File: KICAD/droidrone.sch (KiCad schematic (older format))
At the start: 58 parts, among them IC1 ATMEGA328PB, P1 USB_A, U1 TA4805S, U4 LP2950L-3.3V, Y1 Crystal

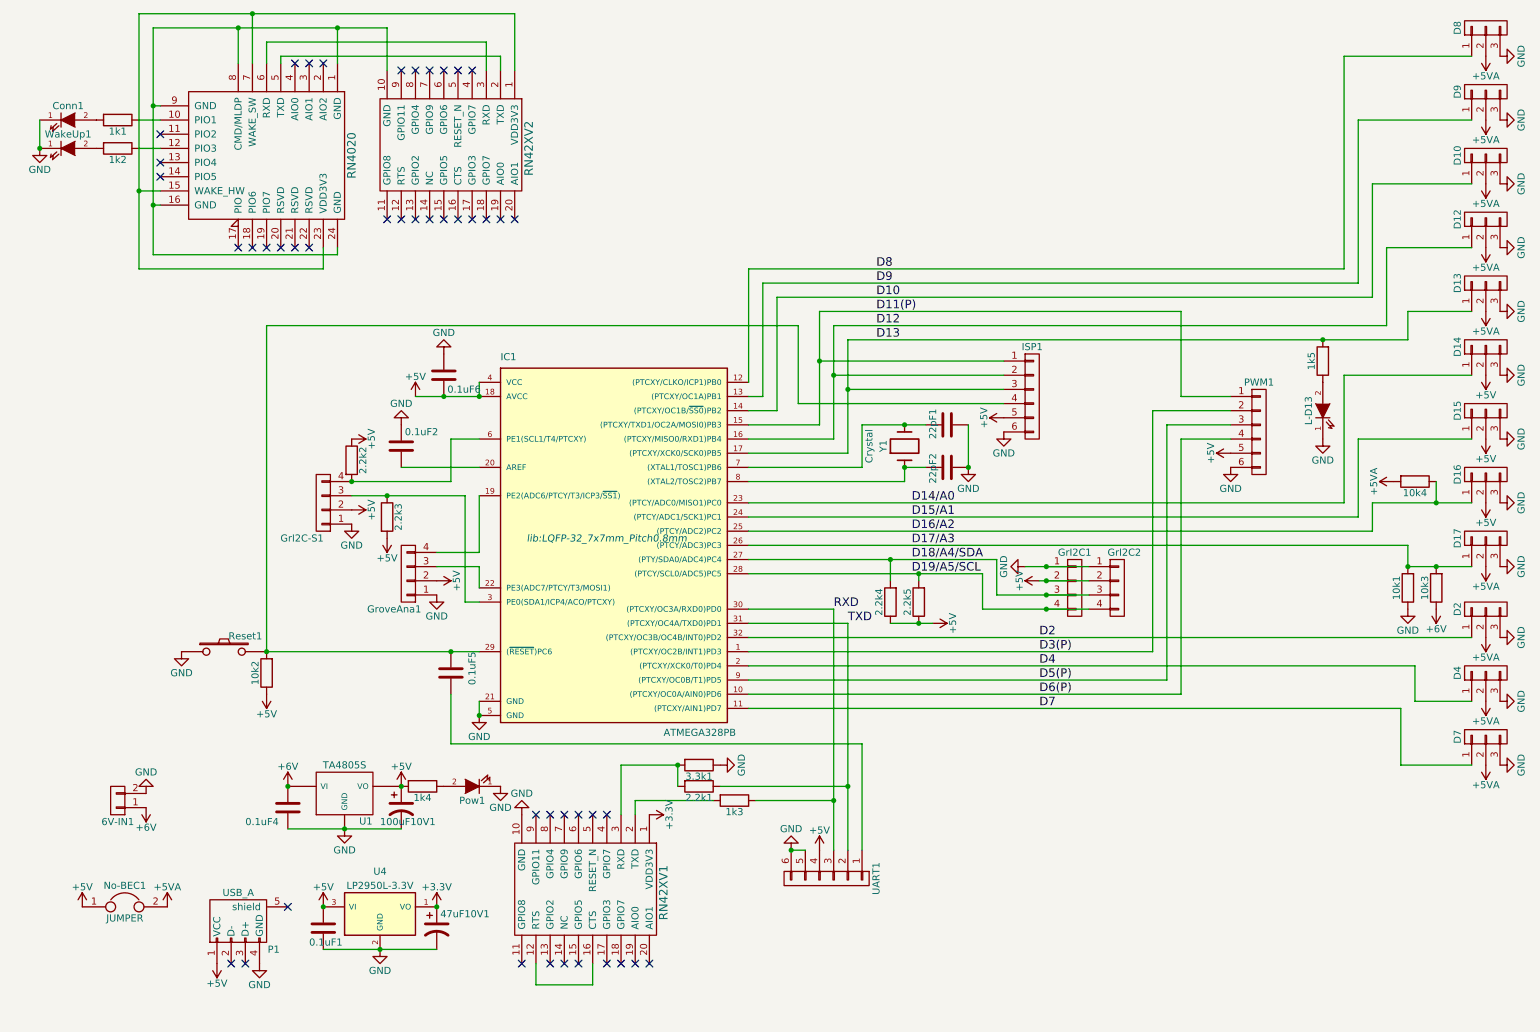
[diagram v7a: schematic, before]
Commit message: add HC-06 BT mod
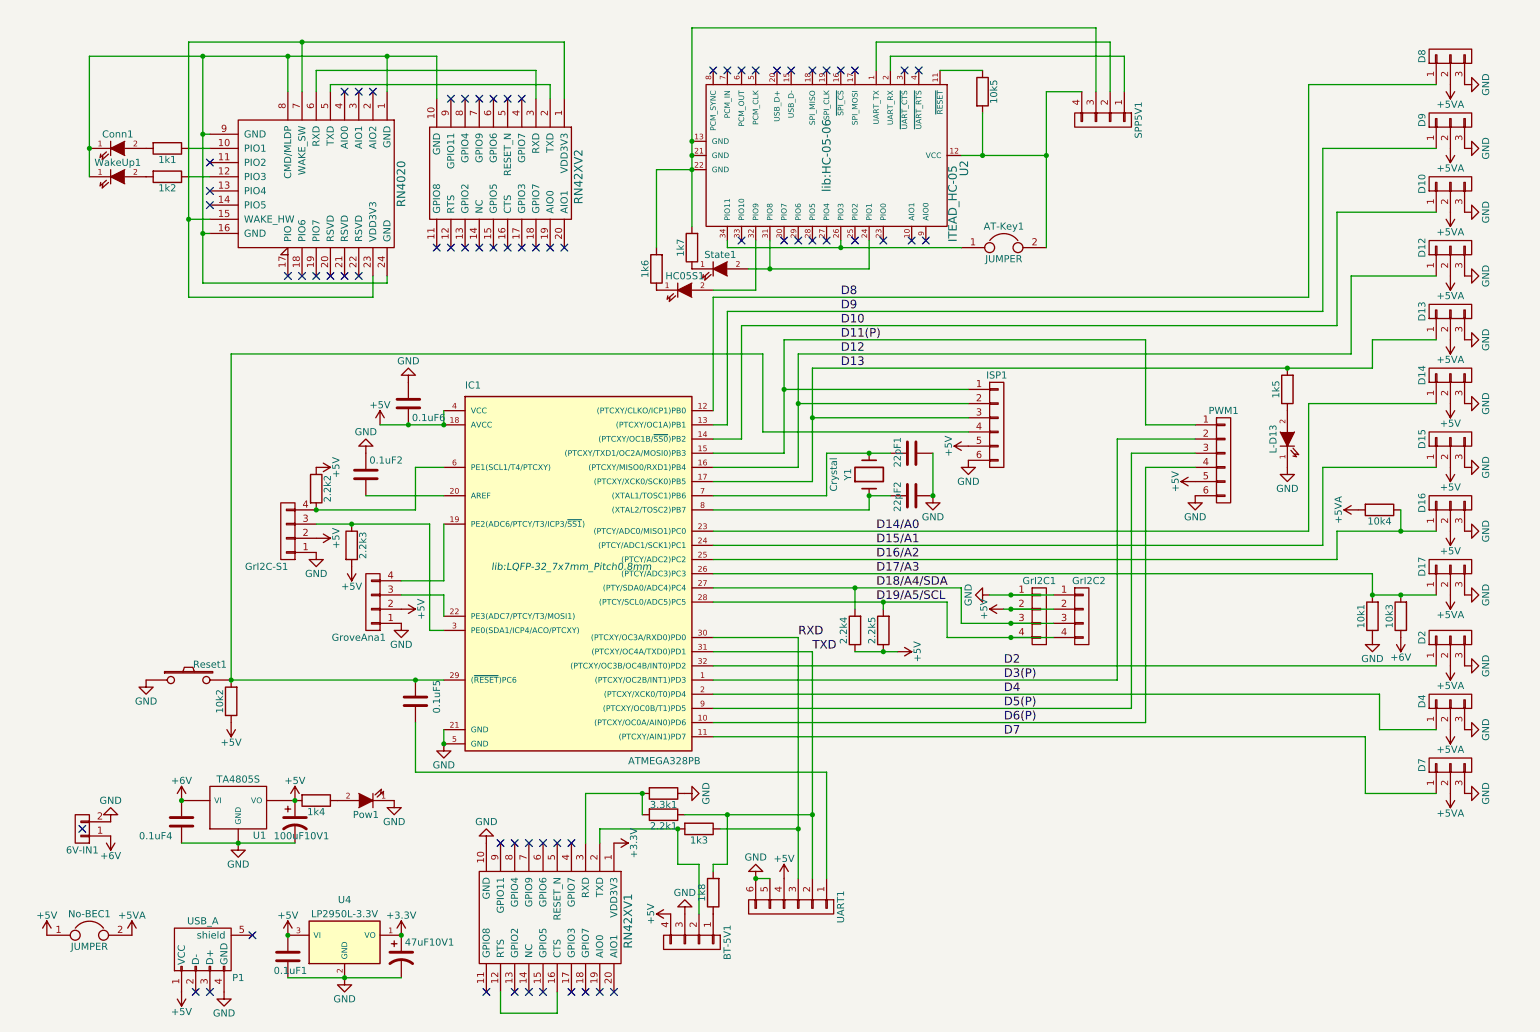
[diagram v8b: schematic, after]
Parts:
- added 10k5: 10k, Resistors_ThroughHole:R_Axial_DIN0204_L3.6mm_D1.6mm_P2.54mm_Vertical, symbol R
- added 1k6, 1k7, 1k8: 1k, Resistors_ThroughHole:R_Axial_DIN0204_L3.6mm_D1.6mm_P2.54mm_Vertical, symbol R
- added AT-Key1: JUMPER, Pin_Headers:Pin_Header_Straight_1x02_Pitch2.54mm, symbol JUMPER
- added BT-5V1, SPP5V1: CONN_01X04, Pin_Headers:Pin_Header_Straight_1x04_Pitch2.54mm, symbol CONN_01X04
- added HC05S1, State1: LED, LEDs:LED_D5.0mm, symbol LED
- added U2: ITEAD_HC-05, lib:HC-05-06, symbol ITEAD_HC-05
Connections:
- net +5V: now also BT-5V1.4 (P4)
- net GND: now also BT-5V1.3 (P3); no longer Conn1.1 (K), WakeUp1.1 (K)
- net TXD: now also 1k8.2
- net at 1k3.2, RN42XV1.2 (TXD): now also BT-5V1.2 (P2)
- net at RN4020.1 (GND), RN4020.16 (GND), RN4020.24 (GND)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: now also Conn1.1 (K), WakeUp1.1 (K)
- new net: SPP5V1.2 (P2), U2.1 (UART_TX)
- new net: 10k5.1, U2.11 (~RESET)
- new net: 10k5.2, AT-Key1.2, SPP5V1.4 (P4), U2.12 (VCC)
- new net: 1k6.2, 1k7.2, SPP5V1.3 (P3), U2.13 (GND), U2.21 (GND), U2.22 (GND)
- new net: SPP5V1.1 (P1), U2.2 (UART_RX)
- new net: State1.2 (A), U2.24 (PIO1), U2.31 (PIO8)
- new net: AT-Key1.1, U2.26 (PIO3), U2.34 (PIO11)
- new net: HC05S1.2 (A), U2.32 (PIO9)
- new net: 1k7.1, State1.1 (K)
- new net: 1k6.1, HC05S1.1 (K)
- new net: 1k8.1, BT-5V1.1 (P1)
- no-connect marks 45 -> 67
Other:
- moved on the sheet: 0.1uF1, 0.1uF2, 0.1uF4, 0.1uF5, 0.1uF6, 100uF10V1, 10k1, 10k2, 10k3, 10k4, 1k1, 1k2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
